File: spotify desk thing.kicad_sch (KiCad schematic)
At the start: 0 parts

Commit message: wired up 3.3v power and usb c
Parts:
- added C1, C6: 10uF, Capacitor_SMD:C_0402_1005Metric, symbol Device:C
- added C19, C2, C3: 0.1uF, Capacitor_SMD:C_0402_1005Metric, symbol Device:C
- added C4: 22uF, Capacitor_SMD:C_0402_1005Metric, symbol Device:C
- added C5: 470uF, Capacitor_SMD:CP_Elec_6.3x5.8, symbol Device:C_Polarized
- added F1: 0603L100SLYR, 0603L100SLYR:FUSC1608X100N, symbol 0603L100SLYR:0603L100SLYR
- added J1: AudioJack3_Ground, symbol Connector_Audio:AudioJack3_Ground
- added J3: USB_C_Receptacle_USB2.0_16P, Connector_USB:USB_C_Receptacle_HRO_TYPE-C-31-M-12, symbol Connector:USB_C_Receptacle_USB2.0_16P
- added L1: 2.2uH, Inductor_SMD:L_0805_2012Metric, symbol Device:L
- added PS1: TPS62162DSGR, TPS62162DSGR:SON50P200X200X80-9N, symbol TPS62162DSGR:TPS62162DSGR
- added R1, R3: 10k, Resistor_SMD:R_0603_1608Metric, symbol Device:R
- added R10, R9: 5.1k, Resistor_SMD:R_0402_1005Metric, symbol Device:R
- added R2: 100k, Resistor_SMD:R_0603_1608Metric, symbol Device:R
- added R4, R5: 27ohm, Resistor_SMD:R_0603_1608Metric, symbol Device:R
- added SW1: RESET, ad-hoc:ALPSALPINE_TopPush_Button, symbol Switch:SW_Push
- added SW2: BOOT, ad-hoc:ALPSALPINE_TopPush_Button, symbol Switch:SW_Push
- added U1: ESP32-S3-WROOM-1-N4, ESP32-S3-WROOM-1-N4:XCVR_ESP32-S3-WROOM-1-N4, symbol ESP32-S3-WROOM-1-N4:ESP32-S3-WROOM-1-N4
- added U2: PCM5242RHBR, RHB32_3P45X3P45_TEX, symbol PCM5242RHBR:PCM5242RHBR
- added U3: EC11E18244A5, EC11E18244A5_ALPS, symbol EC11E:EC11E18244A5
- added U9: USBLC6-2SC6, Package_TO_SOT_SMD:SOT-23-6, symbol Power_Protection:USBLC6-2SC6
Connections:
- new net: R3.2, SW2.2, U1.27 (IO0)
- new net: R5.1, U1.14 (IO20)
- new net: J3.A5 (CC1), R9.2
- new net: PS1.8 (PG), R2.1
- new net: C19.1, R1.2, SW1.2, U1.3 (EN)
- new net: C5.1, F1.2, J3.A4 (VBUS), J3.A9 (VBUS), J3.B4 (VBUS), J3.B9 (VBUS)
- new net: J3.B5 (CC2), R10.2
- new net: R4.1, U1.13 (IO19)
- new net: L1.2, PS1.7 (SW)
- new net 3.3v: C3.1, C4.1, C6.1, L1.1, PS1.6 (VOS), R1.1, R2.2, R3.1, U1.2 (3V3)
- new net 5v: C1.1, C2.1, PS1.2 (VIN), PS1.3 (EN)
- new net GND: C1.2, C19.2, C2.2, C3.2, C4.2, C5.2, C6.2, J1.G, J3.A1 (GND), J3.A12 (GND), J3.B1 (GND), J3.B12 (GND), J3.S1 (SHIELD), PS1.1 (PGND), PS1.4 (AGND), PS1.5 (FB), PS1.9 (EXP), R10.1, R9.1, SW1.1, SW2.1, U1.1 (GND), U1.40 (GND__1), U1.41_1 (GND__2), U1.41_2 (GND__3), U1.41_3 (GND__4), U1.41_4 (GND__5), U1.41_5 (GND__6), U1.41_6 (GND__7), U1.41_7 (GND__8), U1.41_8 (GND__9), U1.41_9 (GND__10), U9.2 (GND)
- new net RAW_D+: J3.A6 (D+), J3.B6 (D+), U9.3 (I/O2)
- new net RAW_D-: J3.A7 (D-), J3.B7 (D-), U9.1 (I/O1)
- new net USB_D+: R5.2, U9.4 (I/O2)
- new net USB_D-: R4.2, U9.6 (I/O1)
- new net VBUS: F1.1, U9.5 (VBUS)
- no-connect marks 0 -> 2

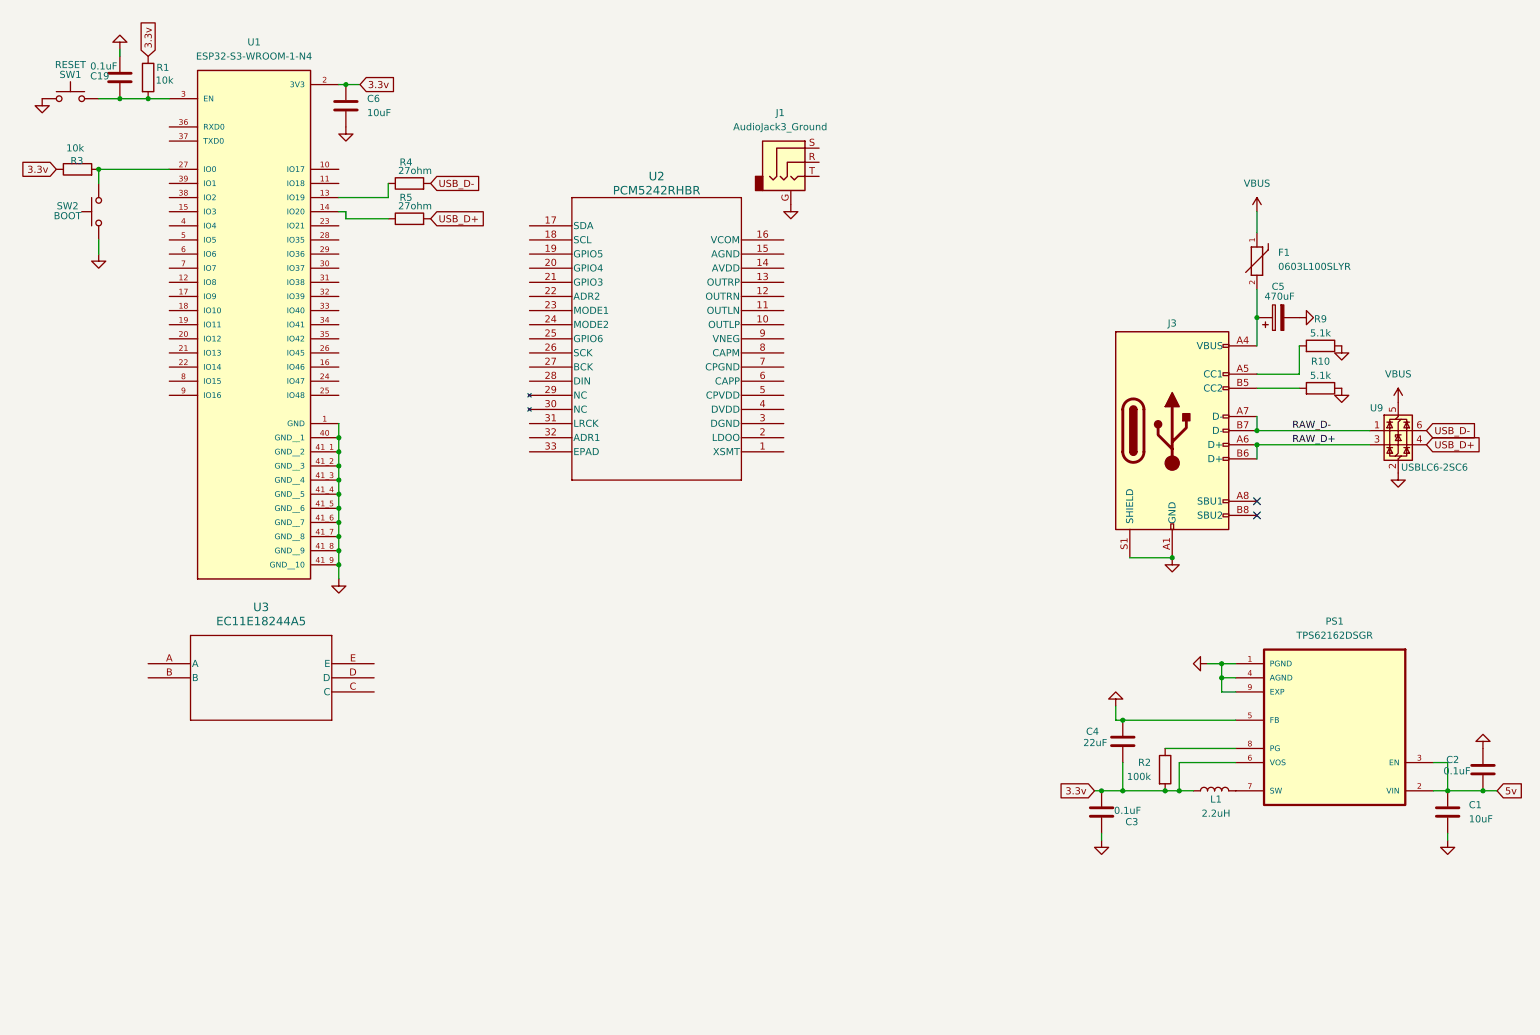
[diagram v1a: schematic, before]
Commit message: moved stuff around and connected lcd/encoder
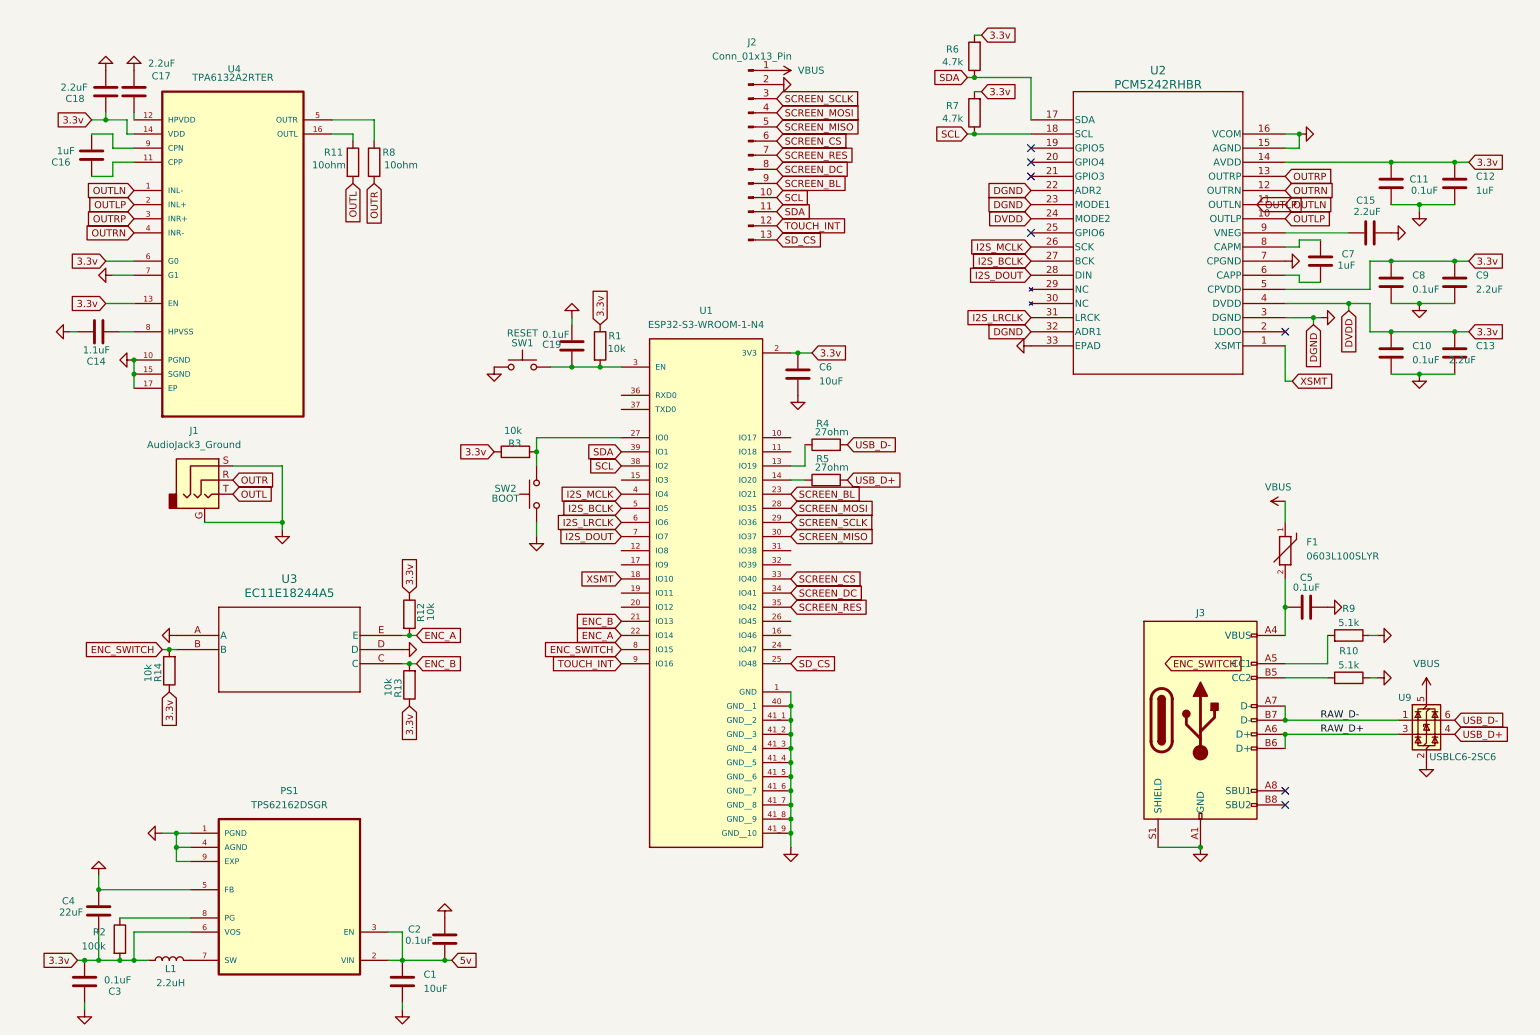
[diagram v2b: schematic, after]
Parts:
- removed C5: 470uF, Capacitor_SMD:CP_Elec_6.3x5.8, symbol Device:C_Polarized
- added C10, C11, C5, C8: 0.1uF, Capacitor_SMD:C_0402_1005Metric, symbol Device:C
- added C12, C16, C7: 1uF, Capacitor_SMD:C_0402_1005Metric, symbol Device:C
- added C13, C15, C17, C18, C9: 2.2uF, Capacitor_SMD:C_0402_1005Metric, symbol Device:C
- added C14: 1.1uF, Capacitor_SMD:C_0402_1005Metric, symbol Device:C
- added J2: Conn_01x13_Pin, symbol Connector:Conn_01x13_Pin
- added R11, R8: 10ohm, Resistor_SMD:R_0603_1608Metric, symbol Device:R
- added R12, R13, R14: 10k, Resistor_SMD:R_0603_1608Metric, symbol Device:R
- added R6, R7: 4.7k, Resistor_SMD:R_0603_1608Metric, symbol Device:R
- added U4: TPA6132A2RTER, TPA6132A2RTER:QFN50P300X300X80-16N, symbol TPA6132A2RTER:TPA6132A2RTER
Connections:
- net 3.3v: now also U2.14 (AVDD), U2.24 (MODE2), U2.4 (DVDD), U2.5 (CPVDD), C10.1, C11.1, C12.1, C13.1, C18.1, C8.1, C9.1, R12.1, R13.1, R14.1, R6.2, R7.2, U4.13 (EN), U4.14 (VDD), U4.6 (G0)
- net GND: now also J1.S, U2.15 (AGND), U2.16 (VCOM), U2.22 (ADR2), U2.23 (MODE1), U2.3 (DGND), U2.32 (ADR1), U2.33 (EPAD), U2.7 (CPGND), U3.A, U3.D, C10.2, C11.2, C12.2, C13.2, C14.1, C15.2, C17.2, C18.2, C5.2, C8.2, C9.2, J2.2 (Pin_2), U4.10 (PGND), U4.15 (SGND), U4.17 (EP), U4.7 (G1)
- net VBUS: now also J2.1 (Pin_1)
- net ENC_SWITCH: now reaches U3.B
- net ENC_SWITCH: now also U1.8 (IO15), R14.2
- net ENC_B: now reaches U3.C
- net ENC_B: now also U1.21 (IO13), R13.2
- net ENC_A: now reaches U3.E
- net ENC_A: now also U1.22 (IO14), R12.2
- net XSMT: now reaches U2.1 (XSMT)
- net XSMT: now also U1.18 (IO10)
- net OUTLP: now reaches U2.10 (OUTLP)
- net OUTLP: now also U4.2 (INL+)
- net OUTLN: now reaches U2.11 (OUTLN)
- net OUTLN: now also U4.1 (INL-)
- net OUTRN: now reaches U2.12 (OUTRN)
- net OUTRN: now also U4.4 (INR-)
- net OUTRP: now reaches U2.13 (OUTRP)
- net OUTRP: now also U4.3 (INR+)
- net SDA: now reaches U2.17 (SDA)
- net SDA: now also U1.39 (IO1), J2.11 (Pin_11), R6.1
- net SCL: now reaches U2.18 (SCL)
- net SCL: now also U1.38 (IO2), J2.10 (Pin_10), R7.1
- net I2S_MCLK: now reaches U2.26 (SCK)
- net I2S_MCLK: now also U1.4 (IO4)
- net I2S_BCLK: now reaches U2.27 (BCK)
- net I2S_BCLK: now also U1.5 (IO5)
- net I2S_DOUT: now reaches U2.28 (DIN)
- net I2S_DOUT: now also U1.7 (IO7)
- net I2S_LRCLK: now reaches U2.31 (LRCK)
- net I2S_LRCLK: now also U1.6 (IO6)
- net at U2.6 (CAPP): now also C7.2
- net at U2.8 (CAPM): now also C7.1
- net at U2.9 (VNEG): now also C15.1
- net OUTR: now reaches J1.R
- net OUTR: now also R8.2
- net OUTL: now reaches J1.T
- net OUTL: now also R11.2
- net at F1.2, J3.A4 (VBUS), J3.A9 (VBUS)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: now also C5.1
- net SCREEN_BL: now reaches U1.23 (IO21)
- net SCREEN_BL: now also J2.9 (Pin_9)
- net SD_CS: now reaches U1.25 (IO48)
- net SD_CS: now also J2.13 (Pin_13)
- net SCREEN_MOSI: now reaches U1.28 (IO35)
- net SCREEN_MOSI: now also J2.4 (Pin_4)
- net SCREEN_SCLK: now reaches U1.29 (IO36)
- net SCREEN_SCLK: now also J2.3 (Pin_3)
- net SCREEN_MISO: now reaches U1.30 (IO37)
- net SCREEN_MISO: now also J2.5 (Pin_5)
- net SCREEN_CS: now reaches U1.33 (IO40)
- net SCREEN_CS: now also J2.6 (Pin_6)
- net SCREEN_DC: now reaches U1.34 (IO41)
- net SCREEN_DC: now also J2.8 (Pin_8)
- net SCREEN_RES: now reaches U1.35 (IO42)
- net SCREEN_RES: now also J2.7 (Pin_7)
- net TOUCH_INT: now reaches U1.9 (IO16)
- net TOUCH_INT: now also J2.12 (Pin_12)
- new net: R11.1, U4.16 (OUTL)
- new net: R8.1, U4.5 (OUTR)
- new net: C16.1, U4.11 (CPP)
- new net: C16.2, U4.9 (CPN)
- new net: C14.2, U4.8 (HPVSS)
- new net: C17.1, U4.12 (HPVDD)
- no-connect marks 2 -> 7
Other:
- company: (none) -> blaze - Hack Club
- title: (none) -> Spotify Desk Thing - Blueprint
- moved on the sheet: C1, C19, C2, C3, C4, C6, F1, J1, J3, L1, PS1, R1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

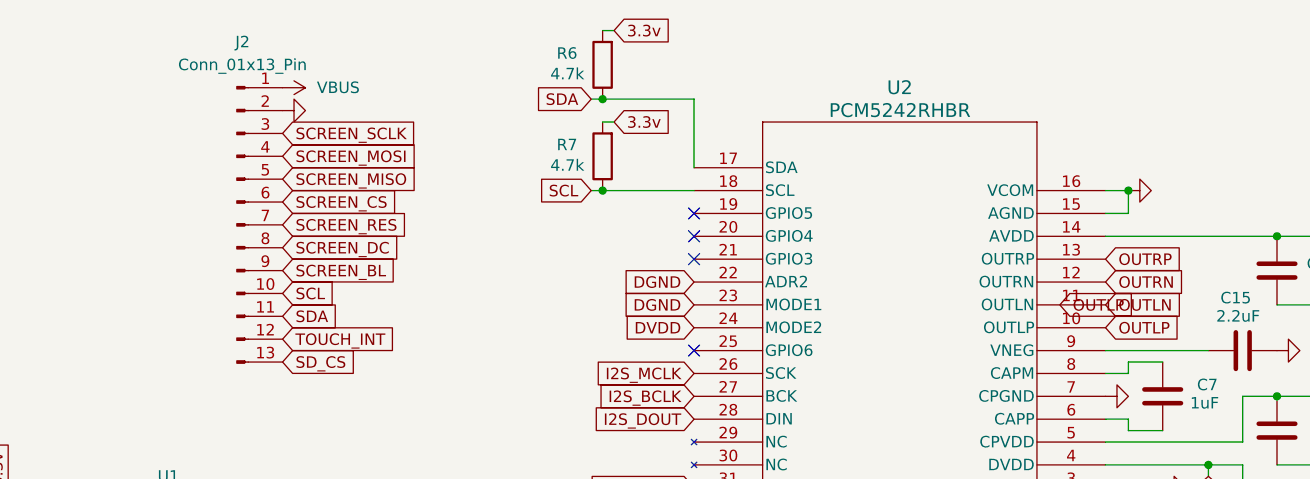
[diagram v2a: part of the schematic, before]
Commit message: deleted unconnected traces
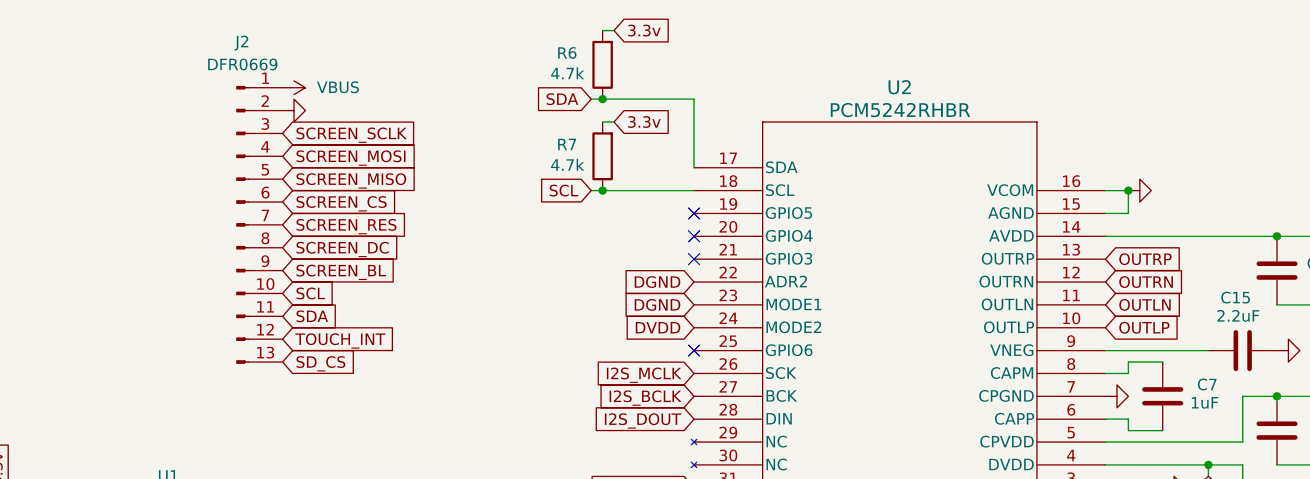
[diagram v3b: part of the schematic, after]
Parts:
- J2: value Conn_01x13_Pin -> DFR0669
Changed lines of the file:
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@@
 		)
 	)
-	(global_label "OUTLP"
-		(shape input)
-		(at 234.95 45.72 0)
-		(fields_autoplaced yes)
-		(effects
-			(font
-				(size 1.27 1.27)
-			)
-			(justify left)
-		)
-		(property "Intersheetrefs" "${INTERSHEET_REFS}"
-			(at 243.8619 45.72 0)
-			(effects
-				(font
-					(size 1.27 1.27)
-				)
-				(justify left)
-				(hide yes)
-			)
-		)
-	)
 	(global_label "3.3v"
 		(shape input)
@@
 			)
 		)
-		(property "Value" "Conn_01x13_Pin"
+		(property "Value" "DFR0669"
 			(at 144.145 19.05 0)
 			(effects

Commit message: routing started
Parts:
- J1: footprint (none) -> Connector_Audio:Jack_3.5mm_CUI_SJ-3524-SMT_Horizontal
- J2: footprint (none) -> Connector_PinHeader_2.54mm:PinHeader_1x13_P2.54mm_Vertical
- U1: footprint ESP32-S3-WROOM-1-N4:XCVR_ESP32-S3-WROOM-1-N4 -> ESP32_S3_WROOM_1_N4:XCVR_ESP32-S3-WROOM-1-N4
- U2: footprint RHB32_3P45X3P45_TEX -> PCM5242RHBR:RHB32_3P45X3P45_TEX
- U4: footprint TPA6132A2RTER:QFN50P300X300X80-16N -> Package_DFN_QFN:WQFN-16-1EP_3x3mm_P0.5mm_EP1.6x1.6mm_ThermalVias
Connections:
- net 5v is gone; now on net VBUS: C1.1, C2.1, PS1.2 (VIN), PS1.3 (EN)
- net ENC_A: now also R14.2, U3.A; no longer R12.2, U3.E
- net ENC_B: now also U3.B; no longer U3.C
- net ENC_SWITCH: now also R12.2, U3.E; no longer R14.2, U3.B
- net GND: now also J1.TN, U2.V, U3.C; no longer J1.G, U3.A
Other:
- moved on the sheet: R13, R14

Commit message: more routing
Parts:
- removed SW1: RESET, ad-hoc:ALPSALPINE_TopPush_Button, symbol Switch:SW_Push
- removed SW2: BOOT, ad-hoc:ALPSALPINE_TopPush_Button, symbol Switch:SW_Push
- added BOOT1: BOOT, EVP_AWED4A:SW_EVP-AWED4A, symbol EVP-AWED4A:EVP-AWED4A
- added RESET1: RESET, EVP_AWED4A:SW_EVP-AWED4A, symbol EVP-AWED4A:EVP-AWED4A
- U4: renamed from U3; footprint EC11E18244A5_ALPS -> EC11E:EC11E18244A5_ALPS
- renumbered C19 to C1, C12 to C10, C7 to C11, C6 to C12, C8 to C15, C11 to C16, C5 to C17, C1 to C18, C2 to C19, C10 to C2, C4 to C3, C18 to C4, C17 to C5, C16 to C6, C15 to C7, C9 to C8, C3 to C9, J2 to J1, J1 to J2, R4 to R1, R11 to R10, R8 to R11, R10 to R13, R9 to R14, R5 to R2, R14 to R3, R13 to R4, R3 to R5, R1 to R6, R6 to R8, R2 to R9, U4 to U2, U2 to U3, U9 to U5
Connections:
- net GND: now also BOOT1.1, RESET1.1
- net at R5.2, U1.27 (IO0): now also BOOT1.2
- net at C1.1, R6.2, U1.3 (EN): now also RESET1.2

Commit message: updated stuff to jlc thing
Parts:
- BOOT1: footprint EVP_AWED4A:SW_EVP-AWED4A -> Button_Switch_SMD:SW_SPST_CK_KMS2xxG; symbol EVP-AWED4A:EVP-AWED4A -> Switch:CK_KMS2xxG; Part # SKHHAMA010 -> KSR211GLFS
- C12: renamed from C14; value 1.1uF -> 1uF; footprint Capacitor_SMD:C_0402_1005Metric -> Capacitor_SMD:C_0603_1608Metric
- J1: renamed from J2; footprint Connector_Audio:Jack_3.5mm_CUI_SJ-3524-SMT_Horizontal -> SJ_3523_SMT_TR:CUI_SJ-3523-SMT-TR; symbol Connector_Audio:AudioJack3_Ground -> SJ-3523-SMT-TR:SJ-3523-SMT-TR; MANUFACTURER (none) -> CUI Inc
- RESET1: footprint EVP_AWED4A:SW_EVP-AWED4A -> Button_Switch_SMD:SW_SPST_CK_KMS2xxG; symbol EVP-AWED4A:EVP-AWED4A -> Switch:CK_KMS2xxG; AVAILABILITY Bad -> (none); DESCRIPTION Tactile Switch SPST-NO Top Actuated Surface Mount -> (none); MF Panasonic -> (none); MP EVP-AWBD2A -> (none); PACKAGE None -> (none); PRICE None -> (none); Part # SKHHAMA010 -> KSR211GLFS
- renumbered C8 to C10, C10 to C11, C9 to C13, C12 to C14, C13 to C15, C15 to C16, C3 to C2, C16 to C3, C2 to C6, C6 to C7, C7 to C8, C11 to C9, J3 to J2, J1 to J3, R2 to R1, R1 to R2, R4 to R3, R3 to R4, R6 to R5, R7 to R6, R5 to R7
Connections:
- net GND: now also BOOT1.SH (B), J1.1 (SLEEVE), RESET1.SH (B); no longer J1.S, J1.TN
- net OUTL: now also J1.2 (TIP); no longer J1.T
- net OUTR: now also J1.3 (RING); no longer J1.R
